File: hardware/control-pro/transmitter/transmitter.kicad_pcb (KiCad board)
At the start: 2 copper layers, 69.1 x 53.8 mm, 10 parts, among them J1 Output, J2 INPUT

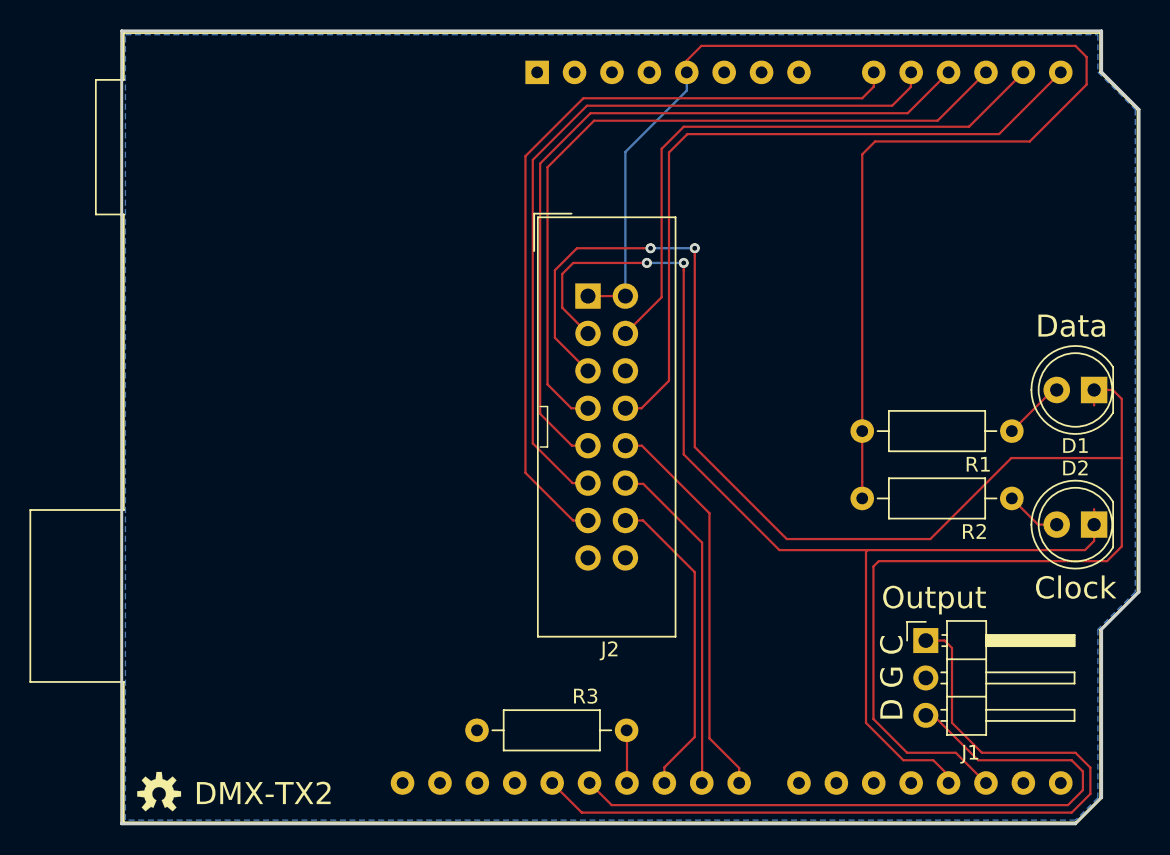
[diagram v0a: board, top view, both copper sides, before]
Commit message: DMX-TX2 V1.1: - Fixed shield footprint - Moved Clock LED to avoid Arduino ICSP connector. - Relabeled the clock fast and slow LED connections in the   schematic to match the board layout. - Added Fcu power plane - Redid Fcu layout - Added rounded corners
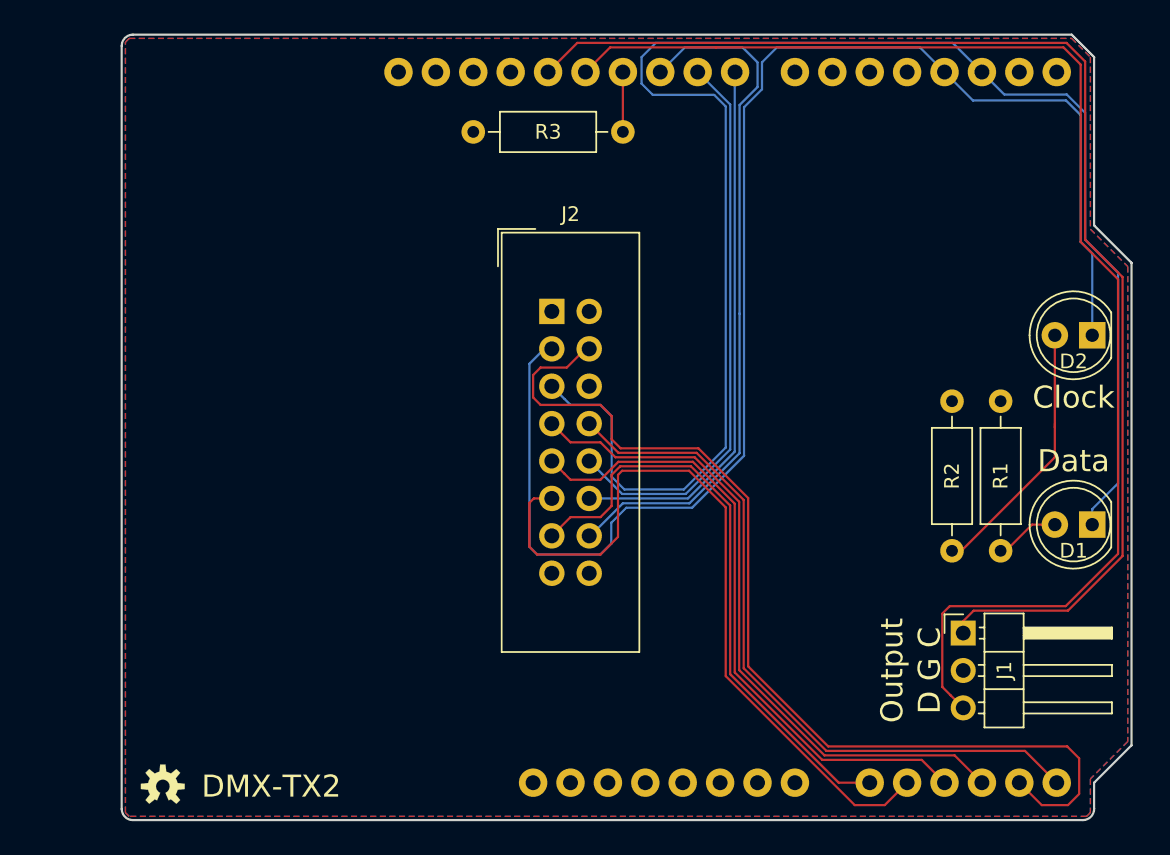
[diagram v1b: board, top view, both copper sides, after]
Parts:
- removed the ? at (118.9, 114.8)
- added ?: , footprints:OSHW-LOGO-S, F.Cu at (119.1, 114.3)
- A1: footprint Module:Arduino_UNO_R3 -> footprints:ARDUINO_R3_NO_HOLES
- moved R3 40.6 mm to (150.4, 69.8)
- moved A1 24.9 mm to (150.6, 89.9)
- moved D2 12.9 mm to (182.2, 83.7)
- moved R1 9.62 mm to (176.0, 88.1), turned to 270 degrees
- moved D1 9.14 mm to (182.2, 96.5)
- moved R2 8.99 mm to (172.7, 88.1), turned to 270 degrees
- moved J2 2.67 mm to (145.5, 82.0)
- moved J1 2.59 mm to (173.5, 103.9)
- moved G*** 0.54 mm to (120.1, 109.5)
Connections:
- A1 pad 23: /~CLK_SLO -> /~CLK_FST
- A1 pad 24: /~CLK_FST -> /~CLK_SLO
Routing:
- net +5V: track 90.6 -> 0.43 mm
- net /RX: track 48.1 -> 89.7 mm
- net /RXCLK: track 57.4 -> 86.5 mm
- net /A4: track 40.3 -> 68.3 mm
- net /~HWD_DT: track 21.3 -> 47.3 mm
- net /~CLOCK: track 78.7 -> 99.2 mm, vias 2 -> 0
- net Net-(D2-Pad2): track 3.78 -> 18.2 mm
- net /~CLK_FST: track 23.2 -> 37.0 mm
- net /A0: track 53.7 -> 40.4 mm
- net /~CLK_SLO: track 26.8 -> 38.3 mm
- net /A2: track 51.4 -> 43.4 mm
- net /A3: track 50.6 -> 46.0 mm
- net /~DATA: track 115.7 -> 112.5 mm, vias 2 -> 0
- net /A5: track 48.1 -> 50.1 mm
- net /A1: track 52.9 -> 52.1 mm
- added copper zone on F.Cu, net +5V
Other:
- board size 69.1 x 53.8 mm -> 68.6 x 53.3 mm
- net class Power added: clearance 0.1524, trace_width 0.3048, via_dia 1.27, via_drill 0.635
- board text added: "DMX-TX2, Rev 1.1 Crazy Giraffe Software"
- board text removed: "DMX-TX2, Rev 1.0 Crazy Giraffe Software"

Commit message: TX2: - Added buffer to drive LEDs - Added decoupling capacitors - Fixed dimmer traces on PCB
DMX-CPC*:
- Switched to horizontal 16 pin connectors since vertical was too tall with a cable plugged in
- Swapped the clock speed and step switches to match the order on the TX1
- Swapped the data and clock LEDs to match the order on the TX1

DMX-CPD*:
- Split dimmer controls out to its own PCB
- Added 2nd 16 pin connector to daisy chain with DMX-CPC*.
- Switched to horizontal 16 pin connectors since vertical was too tall with a cable plugged in

Updated readmes with parts, board links.
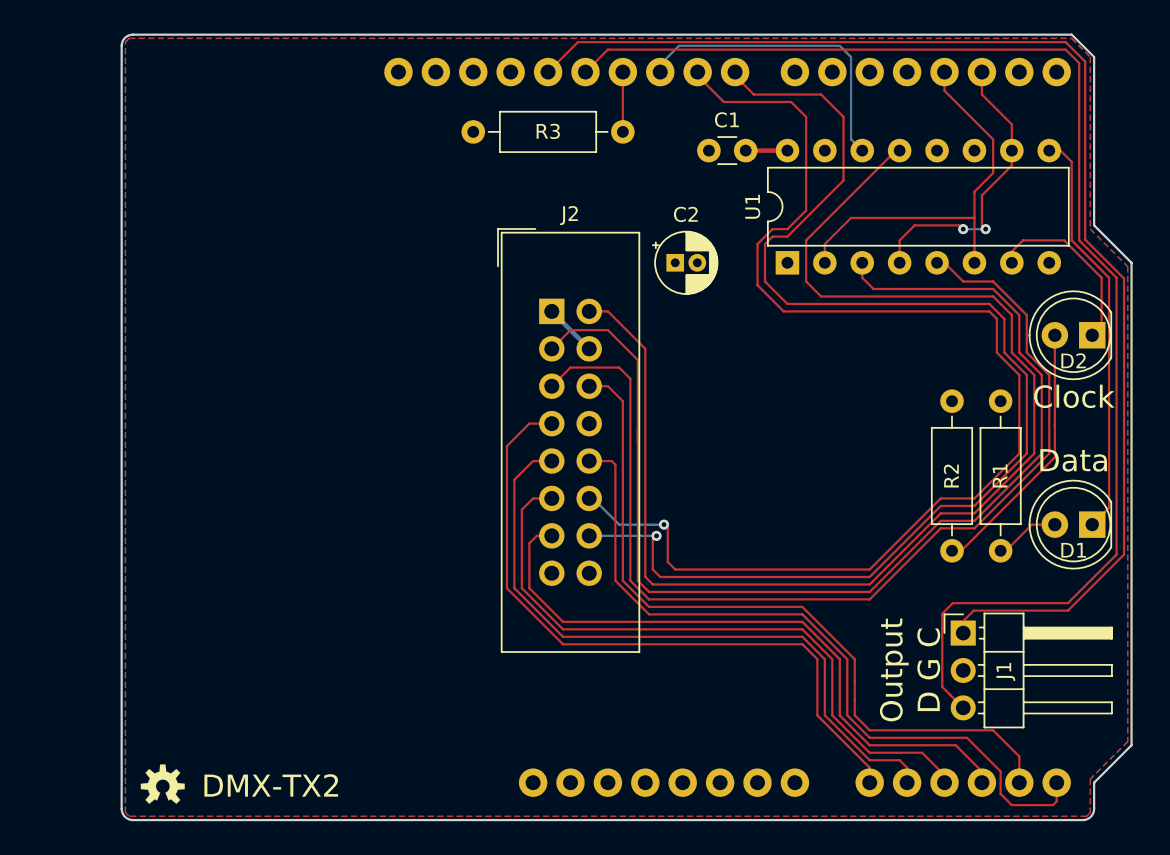
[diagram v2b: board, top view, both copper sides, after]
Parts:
- added C1: 0.1uF, Capacitor_THT:C_Disc_D3.0mm_W1.6mm_P2.50mm, F.Cu at (156.2, 71.1)
- added C2: 10uF, Capacitor_THT:CP_Radial_D4.0mm_P1.50mm, F.Cu at (153.9, 78.7)
- added U1: 74LS365, Package_DIP:DIP-16_W7.62mm, F.Cu at (161.5, 78.7)
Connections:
- A1 pad 17: /~DATA -> /DATA
- A1 pad 18: /~CLOCK -> /CLOCK
- A1 pad 25: /~HWD_DT -> /HWD_DT
- D1 pad 1: /~DATA -> Net-(D1-Pad1)
- D2 pad 1: /~CLOCK -> Net-(D2-Pad1)
- J2 pad 10: /~CLK_SLO -> /A5
- J2 pad 11: /A1 -> /A2
- J2 pad 12: /~CLK_FST -> /~CLK_SLO
- J2 pad 13: /A0 -> /A3
- J2 pad 14: /~HWD_DT -> /~CLK_FST
- J2 pad 2: +5V -> /~HWD_DT
- J2 pad 4: /A4 -> +5V
- J2 pad 6: GND -> /A4
- J2 pad 7: /A3 -> /A0
- J2 pad 8: /A5 -> GND
- J2 pad 9: /A2 -> /A1
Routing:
- net /~CLK_FST: track 37.0 -> 85.9 mm, vias 0 -> 1
- net /~CLK_SLO: track 38.3 -> 85.0 mm, vias 0 -> 1
- net /~DATA: track 112.5 -> 71.3 mm
- net /~HWD_DT: track 47.3 -> 87.3 mm
- net Net-(D1-Pad1): track 0.00 -> 28.0 mm
- net /CLOCK: track 0.00 -> 27.0 mm
- net /~CLOCK: track 99.2 -> 77.6 mm
- net /HWD_DT: track 0.00 -> 21.0 mm
- net /DATA: track 0.00 -> 20.3 mm, vias 0 -> 2
- net /A4: track 68.3 -> 50.8 mm
- net Net-(D2-Pad1): track 0.00 -> 12.6 mm
- net +5V: track 0.43 -> 7.11 mm
- net /A1: track 52.1 -> 45.4 mm
- net /A0: track 40.4 -> 46.3 mm
- net /A3: track 46.0 -> 43.7 mm
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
